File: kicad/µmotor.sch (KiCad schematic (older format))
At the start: 3 parts, among them J101 CAN+PWR

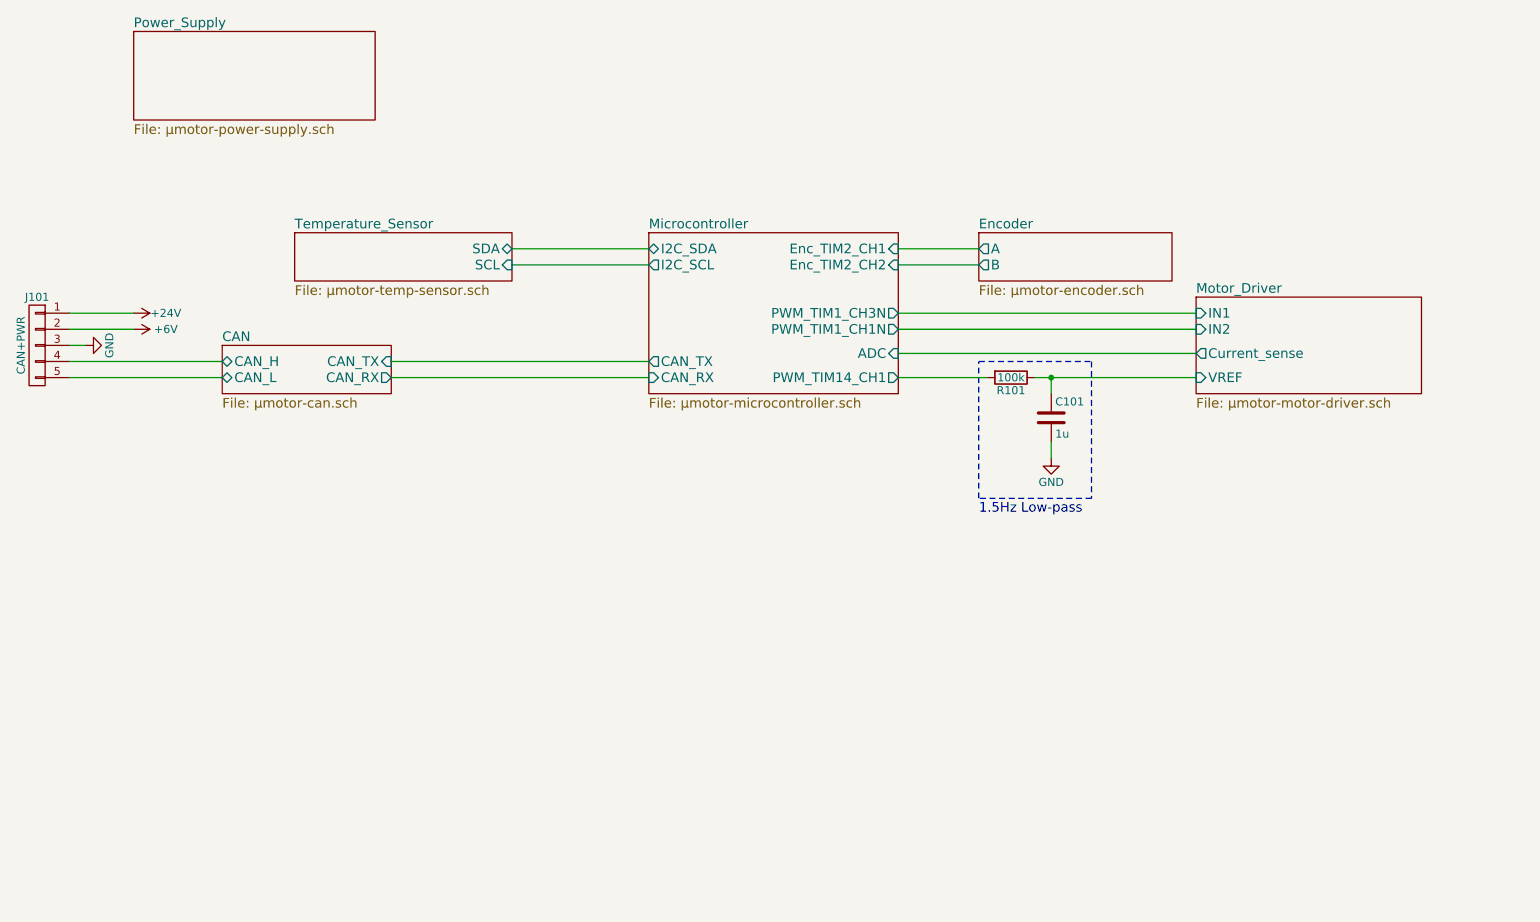
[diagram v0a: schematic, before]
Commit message: second design: STM32L432KC µC with DRV8323S gate driver and FDMD82xx FETs
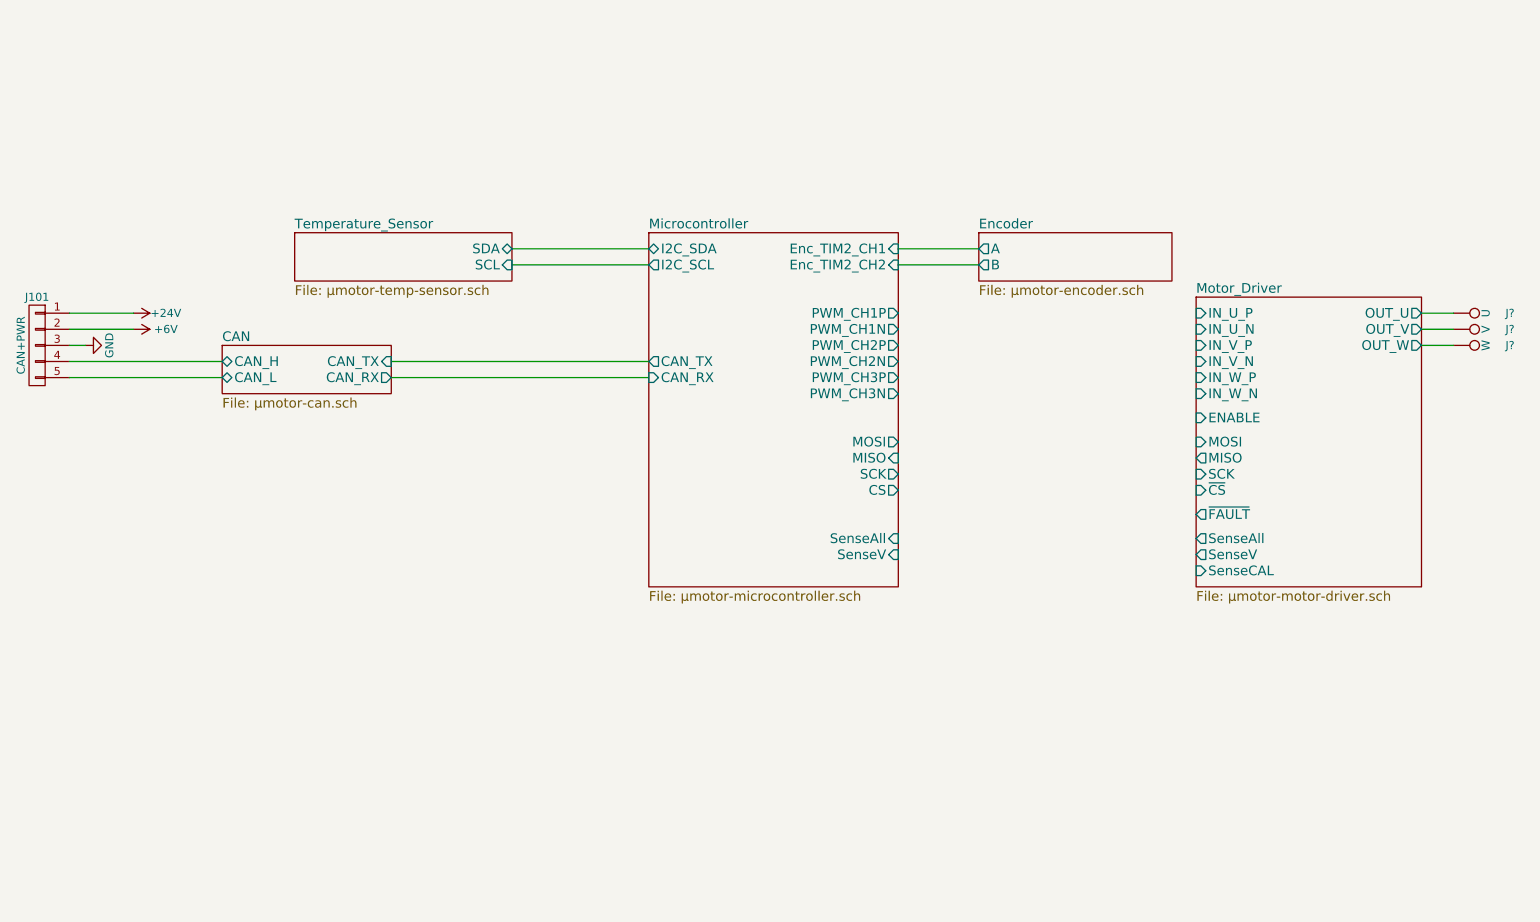
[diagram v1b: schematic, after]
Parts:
- removed C101: 1u, Capacitors_SMD:C_0603, symbol C
- removed R101: 100k, Resistors_SMD:R_0603, symbol R
- added J?: U, Measurement_Points:Measurement_Point_Round-SMD-Pad_Small, symbol TEST_1P
- added J?: V, Measurement_Points:Measurement_Point_Round-SMD-Pad_Small, symbol TEST_1P
- added J?: W, Measurement_Points:Measurement_Point_Round-SMD-Pad_Small, symbol TEST_1P
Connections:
- new net Motor_Driver/OUT_U: J?.1
- new net Motor_Driver/OUT_V: J?.1
- new net Motor_Driver/OUT_W: J?.1
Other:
- note removed: "1.5Hz Low-pass"
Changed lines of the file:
@@
 LIBS:AS5045B
 LIBS:TCAN33x
+LIBS:mic4606
+LIBS:drv8323s
+LIBS:FDMD82xx
 LIBS:µmotor-cache
 EELAYER 25 0
@@
 $Descr A4 11693 8268
 encoding utf-8
-Sheet 1 7
+Sheet 1 6
 Title "µmotor - Micro Motor Controller"
 Date "2017-09-14"
@@
 $EndDescr
 $Sheet
-S 4750 3450 1550 1000
+S 4750 3450 1550 2200
 U 59B9FC4A
 F0 "Microcontroller" 60
@@
 F4 "CAN_RX" I L 4750 4350 60
 F5 "CAN_TX" O L 4750 4250 60
-F6 "PWM_TIM1_CH1N" O R 6300 4050 60
-F7 "PWM_TIM1_CH3N" O R 6300 3950 60
-F8 "Enc_TIM2_CH1" I R 6300 3550 60
-F9 "Enc_TIM2_CH2" I R 6300 3650 60
-F10 "ADC" I R 6300 4200 60
-F11 "PWM_TIM14_CH1" O R 6300 4350 60
-$EndSheet
-$Sheet
-S 1550 2200 1500 550
-U 59B9FC51
-F0 "Power_Supply" 60
-F1 "µmotor-power-supply.sch" 60
+F6 "Enc_TIM2_CH1" I R 6300 3550 60
+F7 "Enc_TIM2_CH2" I R 6300 3650 60
+F8 "PWM_CH1N" O R 6300 4050 60
+F9 "PWM_CH1P" O R 6300 3950 60
+F10 "SCK" O R 6300 4950 60
+F11 "MISO" I R 6300 4850 60
+F12 "MOSI" O R 6300 4750 60
+F13 "CS" O R 6300 5050 60
+F14 "PWM_CH2P" O R 6300 4150 60
+F15 "PWM_CH2N" O R 6300 4250 60
+F16 "PWM_CH3P" O R 6300 4350 60
+F17 "PWM_CH3N" O R 6300 4450 60
+F18 "SenseAll" I R 6300 5350 60
+F19 "SenseV" I R 6300 5450 60
 $EndSheet
 $Sheet
@@
 $EndSheet
 $Sheet
-S 8150 3850 1400 600
+S 8150 3850 1400 1800
 U 59B9FE17
 F0 "Motor_Driver" 60
 F1 "µmotor-motor-driver.sch" 60
-F2 "IN1" I L 8150 3950 60
-F3 "IN2" I L 8150 4050 60
-F4 "VREF" I L 8150 4350 60
-F5 "Current_sense" O L 8150 4200 60
+F2 "IN_U_P" I L 8150 3950 60
+F3 "SenseV" O L 8150 5450 60
+F4 "IN_U_N" I L 8150 4050 60
+F5 "IN_V_P" I L 8150 4150 60
+F6 "IN_V_N" I L 8150 4250 60
+F7 "IN_W_P" I L 8150 4350 60
+F8 "IN_W_N" I L 8150 4450 60
+F9 "SenseCAL" I L 8150 5550 60
+F10 "ENABLE" I L 8150 4600 60
+F11 "MOSI" I L 8150 4750 60
+F12 "MISO" O L 8150 4850 60
+F13 "SCK" I L 8150 4950 60
+F14 "~CS" I L 8150 5050 60
+F15 "OUT_U" O R 9550 3950 60
+F16 "OUT_W" O R 9550 4150 60
+F17 "OUT_V" O R 9550 4050 60
+F18 "~FAULT" O L 8150 5200 60
+F19 "SenseAll" O L 8150 5350 60
 $EndSheet
 $Comp
@@
 Wire Wire Line
 	3900 3550 4750 3550
-$Comp
-L R R101
-U 1 1 59BA90AD
-P 7000 4350
-F 0 "R101" V 7080 4350 50  0000 C CNN
-F 1 "100k" V 7000 4350 50  0000 C CNN
-F 2 "Resistors_SMD:R_0603" V 6930 4350 50  0001 C CNN
-F 3 "" H 7000 4350 50  0001 C CNN
-	1    7000 4350
-	0    1    1    0
-$EndComp
-$Comp
-L C C101
-U 1 1 59BAA0EB
-P 7250 4600
-F 0 "C101" H 7275 4700 50  0000 L CNN
-F 1 "1u" H 7275 4500 50  0000 L CNN
-F 2 "Capacitors_SMD:C_0603" H 7288 4450 50  0001 C CNN
-F 3 "" H 7250 4600 50  0001 C CNN
-	1    7250 4600
-	1    0    0    -1
-$EndComp
-Wire Wire Line
-	6850 4350 6300 4350
-Wire Wire Line
-	7150 4350 8150 4350
-Wire Wire Line
-	7250 4450 7250 4350
-Connection ~ 7250 4350
-$Comp
-L GND #PWR04
-U 1 1 59BAA2C3
-P 7250 4850
-F 0 "#PWR04" H 7250 4600 50  0001 C CNN
-F 1 "GND" H 7250 4700 50  0000 C CNN
-F 2 "" H 7250 4850 50  0001 C CNN
-F 3 "" H 7250 4850 50  0001 C CNN
-	1    7250 4850
-	1    0    0    -1
-$EndComp
-Wire Wire Line
-	7250 4850 7250 4750
-Wire Notes Line
-	6800 4250 7500 4250
-Wire Notes Line
-	7500 4250 7500 5100
-Wire Notes Line
-	7500 5100 6800 5100
-Wire Notes Line
-	6800 5100 6800 4250
-Text Notes 6800 5200 0    60   ~ 0
-1.5Hz Low-pass
-Wire Wire Line
-	6300 4200 8150 4200
-Wire Wire Line
-	8150 4050 6300 4050
-Wire Wire Line
-	6300 3950 8150 3950
 Wire Wire Line
 	6800 3550 6300 3550
 Wire Wire Line
 	6300 3650 6800 3650
+$Comp
+L TEST_1P J?
+U 1 1 5A509596
+P 9750 3950
+F 0 "J?" V 9750 4300 50  0000 C CNN
+F 1 "U" H 9750 4150 50  0000 C CNN
+F 2 "Measurement_Points:Measurement_Point_Round-SMD-Pad_Small" H 9950 3950 50  0001 C CNN
+F 3 "" H 9950 3950 50  0001 C CNN
+	1    9750 3950
+	0    1    1    0
+$EndComp
+$Comp
+L TEST_1P J?
+U 1 1 5A50959D
+P 9750 4050
+F 0 "J?" V 9750 4400 50  0000 C CNN
+F 1 "V" H 9750 4250 50  0000 C CNN
+F 2 "Measurement_Points:Measurement_Point_Round-SMD-Pad_Small" H 9950 4050 50  0001 C CNN
+F 3 "" H 9950 4050 50  0001 C CNN
+	1    9750 4050
+	0    1    1    0
+$EndComp
+$Comp
+L TEST_1P J?
+U 1 1 5A5095A4
+P 9750 4150
+F 0 "J?" V 9750 4500 50  0000 C CNN
+F 1 "W" H 9750 4350 50  0000 C CNN
+F 2 "Measurement_Points:Measurement_Point_Round-SMD-Pad_Small" H 9950 4150 50  0001 C CNN
+F 3 "" H 9950 4150 50  0001 C CNN
+	1    9750 4150
+	0    1    1    0
+$EndComp
+Wire Wire Line
+	9750 3950 9550 3950
+Wire Wire Line
+	9550 4050 9750 4050
+Wire Wire Line
+	9750 4150 9550 4150
 $EndSCHEMATC

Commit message: update µC pinout, motor driver, CubeMX, add 3V3 regulator and temperature sensor
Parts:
- added C?: 1µ 16V, symbol C
- added C?: 1µ 6V3, symbol C
- added U?: NCP4623HMX033TCG, symbol NCP4623HMX
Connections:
- net +6V: now also C?.1, U?.1 (IN), U?.4 (CE)
- net GND: now also C?.2, C?.2, U?.6 (GND), U?.7 (GND)
- new net 3V3_CAN: C?.1, U?.3 (OUT)

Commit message: layout: components placed
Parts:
- added J105: U, Measurement_Point_Round-SMD-Pad_Smaller:Measurement_Point_Round-SMD-Pad_Smaller_0.75mm, symbol TEST_1P
- added J106: V, Measurement_Point_Round-SMD-Pad_Smaller:Measurement_Point_Round-SMD-Pad_Smaller_0.75mm, symbol TEST_1P
- added J107: W, Measurement_Point_Round-SMD-Pad_Smaller:Measurement_Point_Round-SMD-Pad_Smaller_0.75mm, symbol TEST_1P
- C101, C102: renamed from C?; footprint (none) -> Capacitors_SMD:C_0603
- J102, J103, J104: renamed from J?; footprint Measurement_Points:Measurement_Point_Round-SMD-Pad_Small -> Measurement_Points:Measurement_Point_Round-TH_Small
- U101: renamed from U?; footprint (none) -> Housings_DFN_QFN:DFN-6-1EP_2x2mm_Pitch0.5mm
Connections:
- net 3V3_CAN renamed +3V3
- new net Microcontroller/HallU: J105.1
- new net Microcontroller/HallV: J106.1
- new net Microcontroller/HallW: J107.1
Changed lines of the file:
@@
 LIBS:conn
 LIBS:linear
-LIBS:regul
-LIBS:74xx
-LIBS:cmos4000
-LIBS:adc-dac
-LIBS:memory
-LIBS:xilinx
-LIBS:microcontrollers
-LIBS:dsp
-LIBS:microchip
-LIBS:analog_switches
-LIBS:motorola
 LIBS:texas
-LIBS:intel
-LIBS:audio
 LIBS:interface
-LIBS:digital-audio
-LIBS:philips
-LIBS:display
-LIBS:cypress
-LIBS:siliconi
-LIBS:opto
-LIBS:atmel
 LIBS:contrib
 LIBS:valves
-LIBS:stm32
 LIBS:DRV8870
 LIBS:INA180A
@@
 LIBS:ncp4623
 LIBS:TMP006
+LIBS:stm32
 LIBS:µmotor-cache
 EELAYER 25 0
@@
 F2 "A" O L 6800 3550 60
 F3 "B" O L 6800 3650 60
-F4 "3V_IN" I R 8000 3550 60
 $EndSheet
 $Sheet
@@
 	1550 4050 1150 4050
 $Sheet
-S 2100 4150 1050 400
+S 2100 4150 1050 300
 U 59B9FE58
 F0 "CAN" 60
@@
 F4 "CAN_H" B L 2100 4250 60
 F5 "CAN_L" B L 2100 4350 60
-F6 "3V_IN" I L 2100 4450 60
 $EndSheet
 Wire Wire Line
@@
 	6300 3650 6800 3650
 $Comp
-L TEST_1P J?
+L TEST_1P J102
 U 1 1 5A509596
 P 9750 3950
-F 0 "J?" V 9750 4300 50  0000 C CNN
+F 0 "J102" V 9750 4300 50  0000 C CNN
 F 1 "U" H 9750 4150 50  0000 C CNN
-F 2 "Measurement_Points:Measurement_Point_Round-SMD-Pad_Small" H 9950 3950 50  0001 C CNN
+F 2 "Measurement_Points:Measurement_Point_Round-TH_Small" H 9950 3950 50  0001 C CNN
 F 3 "" H 9950 3950 50  0001 C CNN
 	1    9750 3950
@@
 $EndComp
 $Comp
-L TEST_1P J?
+L TEST_1P J103
 U 1 1 5A50959D
 P 9750 4050
-F 0 "J?" V 9750 4400 50  0000 C CNN
+F 0 "J103" V 9750 4400 50  0000 C CNN
 F 1 "V" H 9750 4250 50  0000 C CNN
-F 2 "Measurement_Points:Measurement_Point_Round-SMD-Pad_Small" H 9950 4050 50  0001 C CNN
+F 2 "Measurement_Points:Measurement_Point_Round-TH_Small" H 9950 4050 50  0001 C CNN
 F 3 "" H 9950 4050 50  0001 C CNN
 	1    9750 4050
@@
 $EndComp
 $Comp
-L TEST_1P J?
+L TEST_1P J104
 U 1 1 5A5095A4
 P 9750 4150
-F 0 "J?" V 9750 4500 50  0000 C CNN
+F 0 "J104" V 9750 4500 50  0000 C CNN
 F 1 "W" H 9750 4350 50  0000 C CNN
-F 2 "Measurement_Points:Measurement_Point_Round-SMD-Pad_Small" H 9950 4150 50  0001 C CNN
+F 2 "Measurement_Points:Measurement_Point_Round-TH_Small" H 9950 4150 50  0001 C CNN
 F 3 "" H 9950 4150 50  0001 C CNN
 	1    9750 4150
@@
 	9750 4150 9550 4150
 $Comp
-L NCP4623HMX U?
+L NCP4623HMX U101
 U 1 1 5A7689A2
 P 2100 5450
-F 0 "U?" H 2100 5750 50  0000 C CNN
+F 0 "U101" H 2100 5750 50  0000 C CNN
 F 1 "NCP4623HMX033TCG" H 2100 5650 50  0000 C CNN
-F 2 "" H 2100 5450 60  0001 C CNN
+F 2 "Housings_DFN_QFN:DFN-6-1EP_2x2mm_Pitch0.5mm" H 2100 5450 60  0001 C CNN
 F 3 "" H 2100 5450 50  0000 C CNN
 	1    2100 5450
@@
 $EndComp
 $Comp
-L +6V #PWR?
+L +6V #PWR04
 U 1 1 5A768B01
 P 1000 5400
-F 0 "#PWR?" H 1000 5250 50  0001 C CNN
+F 0 "#PWR04" H 1000 5250 50  0001 C CNN
 F 1 "+6V" H 1000 5540 50  0000 C CNN
 F 2 "" H 1000 5400 50  0001 C CNN
@@
 $EndComp
 $Comp
-L C C?
+L C C101
 U 1 1 5A768C33
 P 1350 5750
-F 0 "C?" H 1375 5850 50  0000 L CNN
+F 0 "C101" H 1375 5850 50  0000 L CNN
 F 1 "1µ 16V" H 1375 5650 50  0000 L CNN
-F 2 "" H 1388 5600 50  0001 C CNN
+F 2 "Capacitors_SMD:C_0603" H 1388 5600 50  0001 C CNN
 F 3 "" H 1350 5750 50  0001 C CNN
 	1    1350 5750
@@
 $EndComp
 $Comp
-L C C?
+L C C102
 U 1 1 5A769218
 P 2850 5750
-F 0 "C?" H 2875 5850 50  0000 L CNN
+F 0 "C102" H 2875 5850 50  0000 L CNN
 F 1 "1µ 6V3" H 2875 5650 50  0000 L CNN
-F 2 "" H 2888 5600 50  0001 C CNN
+F 2 "Capacitors_SMD:C_0603" H 2888 5600 50  0001 C CNN
 F 3 "" H 2850 5750 50  0001 C CNN
 	1    2850 5750
@@
 	2850 5400 2850 5600
 $Comp
-L GND #PWR?
+L GND #PWR05
 U 1 1 5A769C21
 P 2050 6100
-F 0 "#PWR?" H 2050 5850 50  0001 C CNN
+F 0 "#PWR05" H 2050 5850 50  0001 C CNN
 F 1 "GND" H 2050 5950 50  0000 C CNN
 F 2 "" H 2050 6100 50  0001 C CNN
@@
 	2850 6000 2850 5900
 Connection ~ 2850 5400
-Text Label 3150 5400 2    60   ~ 0
-3V3_CAN
-Text Label 1650 4450 0    60   ~ 0
-3V3_CAN
-Wire Wire Line
-	1650 4450 2100 4450
 $Sheet
 S 4750 3450 1550 2500
@@
 F22 "GpioB2" B R 6300 5750 60
 F23 "GpioB7" B R 6300 5850 60
+F24 "HallU" I L 4750 5250 60
+F25 "HallV" I L 4750 5350 60
+F26 "HallW" I L 4750 5450 60
 $EndSheet
 Wire Wire Line
@@
 Wire Wire Line
 	7350 5200 8150 5200
-Text Label 8500 3550 2    60   ~ 0
-3V3_CAN
-Wire Wire Line
-	8500 3550 8000 3550
+$Comp
+L +3V3 #PWR06
+U 1 1 5A775FAA
+P 3150 5400
+F 0 "#PWR06" H 3150 5250 50  0001 C CNN
+F 1 "+3V3" H 3150 5540 50  0000 C CNN
+F 2 "" H 3150 5400 50  0001 C CNN
+F 3 "" H 3150 5400 50  0001 C CNN
+	1    3150 5400
+	0    1    1    0
+$EndComp
+$Comp
+L TEST_1P J105
+U 1 1 5A77D176
+P 4550 5250
+F 0 "J105" V 4550 5600 50  0000 C CNN
+F 1 "U" H 4550 5450 50  0000 C CNN
+F 2 "Measurement_Point_Round-SMD-Pad_Smaller:Measurement_Point_Round-SMD-Pad_Smaller_0.75mm" H 4750 5250 50  0001 C CNN
+F 3 "" H 4750 5250 50  0001 C CNN
+	1    4550 5250
+	0    -1   -1   0
+$EndComp
+$Comp
+L TEST_1P J106
+U 1 1 5A77D554
+P 4550 5350
+F 0 "J106" V 4550 5700 50  0000 C CNN
+F 1 "V" H 4550 5550 50  0000 C CNN
+F 2 "Measurement_Point_Round-SMD-Pad_Smaller:Measurement_Point_Round-SMD-Pad_Smaller_0.75mm" H 4750 5350 50  0001 C CNN
+F 3 "" H 4750 5350 50  0001 C CNN
+	1    4550 5350
+	0    -1   -1   0
+$EndComp
+$Comp
+L TEST_1P J107
+U 1 1 5A77D6B7
+P 4550 5450
+F 0 "J107" V 4550 5800 50  0000 C CNN
+F 1 "W" H 4550 5650 50  0000 C CNN
+F 2 "Measurement_Point_Round-SMD-Pad_Smaller:Measurement_Point_Round-SMD-Pad_Smaller_0.75mm" H 4750 5450 50  0001 C CNN
+F 3 "" H 4750 5450 50  0001 C CNN
+	1    4550 5450
+	0    -1   -1   0
+$EndComp
+Wire Wire Line
+	4550 5250 4750 5250
+Wire Wire Line
+	4750 5350 4550 5350
+Wire Wire Line
+	4550 5450 4750 5450
 $EndSCHEMATC

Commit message: layout: minor improvements
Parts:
- added C103: 1µ 16V, Capacitors_SMD:C_0603, symbol C
- added C104: 1µ 6V3, Capacitors_SMD:C_0603, symbol C
- added J108: 5V, Measurement_Point_Round-SMD-Pad_Smaller:Measurement_Point_Round-SMD-Pad_Smaller_0.75mm, symbol TEST_1P
- added J110: IO, Measurement_Point_Round-SMD-Pad_Smaller:Measurement_Point_Round-SMD-Pad_Smaller_0.75mm, symbol TEST_1P
- added U102: NCP4623HMX050TCG, Housings_DFN_QFN:DFN-6-1EP_2x2mm_Pitch0.5mm, symbol NCP4623HMX
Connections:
- net +6V: now also C103.1, U102.1 (IN), U102.4 (CE)
- net GND: now also C103.2, C104.2, U102.6 (GND), U102.7 (GND)
- new net +5V: C104.1, J108.1, U102.3 (OUT)
- new net Microcontroller/GpioC14: J110.1
- no-connect marks 0 -> 1
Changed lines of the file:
@@
 F25 "HallV" I L 4750 5350 60
 F26 "HallW" I L 4750 5450 60
+F27 "GpioC14" B L 4750 5750 60
+F28 "GpioC13" B L 4750 5650 60
 $EndSheet
 Wire Wire Line
@@
 Wire Wire Line
 	4550 5450 4750 5450
+$Comp
+L NCP4623HMX U102
+U 1 1 5A77E49D
+P 2100 6800
+F 0 "U102" H 2100 7100 50  0000 C CNN
+F 1 "NCP4623HMX050TCG" H 2100 7000 50  0000 C CNN
+F 2 "Housings_DFN_QFN:DFN-6-1EP_2x2mm_Pitch0.5mm" H 2100 6800 60  0001 C CNN
+F 3 "" H 2100 6800 50  0000 C CNN
+	1    2100 6800
+	1    0    0    -1
+$EndComp
+$Comp
+L +6V #PWR07
+U 1 1 5A77E4A3
+P 1000 6750
+F 0 "#PWR07" H 1000 6600 50  0001 C CNN
+F 1 "+6V" H 1000 6890 50  0000 C CNN
+F 2 "" H 1000 6750 50  0001 C CNN
+F 3 "" H 1000 6750 50  0001 C CNN
+	1    1000 6750
+	0    -1   -1   0
+$EndComp
+$Comp
+L C C103
+U 1 1 5A77E4A9
+P 1350 7100
+F 0 "C103" H 1375 7200 50  0000 L CNN
+F 1 "1µ 16V" H 1375 7000 50  0000 L CNN
+F 2 "Capacitors_SMD:C_0603" H 1388 6950 50  0001 C CNN
+F 3 "" H 1350 7100 50  0001 C CNN
+	1    1350 7100
+	1    0    0    -1
+$EndComp
+$Comp
+L C C104
+U 1 1 5A77E4AF
+P 2850 7100
+F 0 "C104" H 2875 7200 50  0000 L CNN
+F 1 "1µ 6V3" H 2875 7000 50  0000 L CNN
+F 2 "Capacitors_SMD:C_0603" H 2888 6950 50  0001 C CNN
+F 3 "" H 2850 7100 50  0001 C CNN
+	1    2850 7100
+	1    0    0    -1
+$EndComp
+Wire Wire Line
+	1000 6750 1650 6750
+Wire Wire Line
+	1350 6950 1350 6750
+Connection ~ 1350 6750
+Wire Wire Line
+	1650 6850 1550 6850
+Wire Wire Line
+	1550 6850 1550 6750
+Connection ~ 1550 6750
+Wire Wire Line
+	2550 6750 3150 6750
+Wire Wire Line
+	2850 6750 2850 6950
+$Comp
+L GND #PWR08
+U 1 1 5A77E4BD
+P 2050 7450
+F 0 "#PWR08" H 2050 7200 50  0001 C CNN
+F 1 "GND" H 2050 7300 50  0000 C CNN
+F 2 "" H 2050 7450 50  0001 C CNN
+F 3 "" H 2050 7450 50  0001 C CNN
+	1    2050 7450
+	1    0    0    -1
+$EndComp
+Wire Wire Line
+	2050 7450 2050 7100
+Wire Wire Line
+	1350 7250 1350 7350
+Wire Wire Line
+	1350 7350 2850 7350
+Connection ~ 2050 7350
+Wire Wire Line
+	2850 7350 2850 7250
+Connection ~ 2850 6750
+$Comp
+L +5V #PWR09
+U 1 1 5A77E77B
+P 3150 6750
+F 0 "#PWR09" H 3150 6600 50  0001 C CNN
+F 1 "+5V" H 3150 6890 50  0000 C CNN
+F 2 "" H 3150 6750 50  0001 C CNN
+F 3 "" H 3150 6750 50  0001 C CNN
+	1    3150 6750
+	0    1    1    0
+$EndComp
+$Comp
+L TEST_1P J108
+U 1 1 5A7826F1
+P 3050 6650
+F 0 "J108" V 3050 7000 50  0000 C CNN
+F 1 "5V" H 3050 6850 50  0000 C CNN
+F 2 "Measurement_Point_Round-SMD-Pad_Smaller:Measurement_Point_Round-SMD-Pad_Smaller_0.75mm" H 3250 6650 50  0001 C CNN
+F 3 "" H 3250 6650 50  0001 C CNN
+	1    3050 6650
+	1    0    0    -1
+$EndComp
+Wire Wire Line
+	3050 6650 3050 6750
+Connection ~ 3050 6750
+$Comp
+L TEST_1P J110
+U 1 1 5A784EEF
+P 4550 5750
+F 0 "J110" V 4550 6100 50  0000 C CNN
+F 1 "IO" H 4550 5950 50  0000 C CNN
+F 2 "Measurement_Point_Round-SMD-Pad_Smaller:Measurement_Point_Round-SMD-Pad_Smaller_0.75mm" H 4750 5750 50  0001 C CNN
+F 3 "" H 4750 5750 50  0001 C CNN
+	1    4550 5750
+	0    -1   -1   0
+$EndComp
+Wire Wire Line
+	4750 5750 4550 5750
+NoConn ~ 4750 5650
 $EndSCHEMATC

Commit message: layout: improvements and silkscreen
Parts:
- added J109: 3V3, Measurement_Point_Round-SMD-Pad_Smaller:Measurement_Point_Round-SMD-Pad_Smaller_0.75mm, symbol TEST_1P
- added J111: GND, Measurement_Point_Round-SMD-Pad_Smaller:Measurement_Point_Round-SMD-Pad_Smaller_0.75mm, symbol TEST_1P
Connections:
- net +3V3: now also J109.1
- net GND: now also J111.1
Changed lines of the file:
@@
 	4750 5750 4550 5750
 NoConn ~ 4750 5650
+$Comp
+L TEST_1P J111
+U 1 1 5A786EB9
+P 4000 5350
+F 0 "J111" V 4000 5700 50  0000 C CNN
+F 1 "GND" H 4000 5550 50  0000 C CNN
+F 2 "Measurement_Point_Round-SMD-Pad_Smaller:Measurement_Point_Round-SMD-Pad_Smaller_0.75mm" H 4200 5350 50  0001 C CNN
+F 3 "" H 4200 5350 50  0001 C CNN
+	1    4000 5350
+	1    0    0    -1
+$EndComp
+$Comp
+L TEST_1P J109
+U 1 1 5A7870AB
+P 3800 5350
+F 0 "J109" V 3800 5700 50  0000 C CNN
+F 1 "3V3" H 3800 5550 50  0000 C CNN
+F 2 "Measurement_Point_Round-SMD-Pad_Smaller:Measurement_Point_Round-SMD-Pad_Smaller_0.75mm" H 4000 5350 50  0001 C CNN
+F 3 "" H 4000 5350 50  0001 C CNN
+	1    3800 5350
+	1    0    0    -1
+$EndComp
+$Comp
+L +3V3 #PWR010
+U 1 1 5A78722B
+P 3800 5450
+F 0 "#PWR010" H 3800 5300 50  0001 C CNN
+F 1 "+3V3" H 3800 5590 50  0000 C CNN
+F 2 "" H 3800 5450 50  0001 C CNN
+F 3 "" H 3800 5450 50  0001 C CNN
+	1    3800 5450
+	-1   0    0    1
+$EndComp
+$Comp
+L GND #PWR011
+U 1 1 5A7873A5
+P 4000 5450
+F 0 "#PWR011" H 4000 5200 50  0001 C CNN
+F 1 "GND" H 4000 5300 50  0000 C CNN
+F 2 "" H 4000 5450 50  0001 C CNN
+F 3 "" H 4000 5450 50  0001 C CNN
+	1    4000 5450
+	1    0    0    -1
+$EndComp
+Wire Wire Line
+	3800 5350 3800 5450
+Wire Wire Line
+	4000 5450 4000 5350
 $EndSCHEMATC
